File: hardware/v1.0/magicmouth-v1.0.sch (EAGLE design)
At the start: 36 parts, among them IC1 LM386N, IC2 ATMEGA328P_PDIP, J2 AUDIO-JACK2PTH, Q1 16Mhz, U1 ARDUINOR3-NOIOREF-NOTEXT

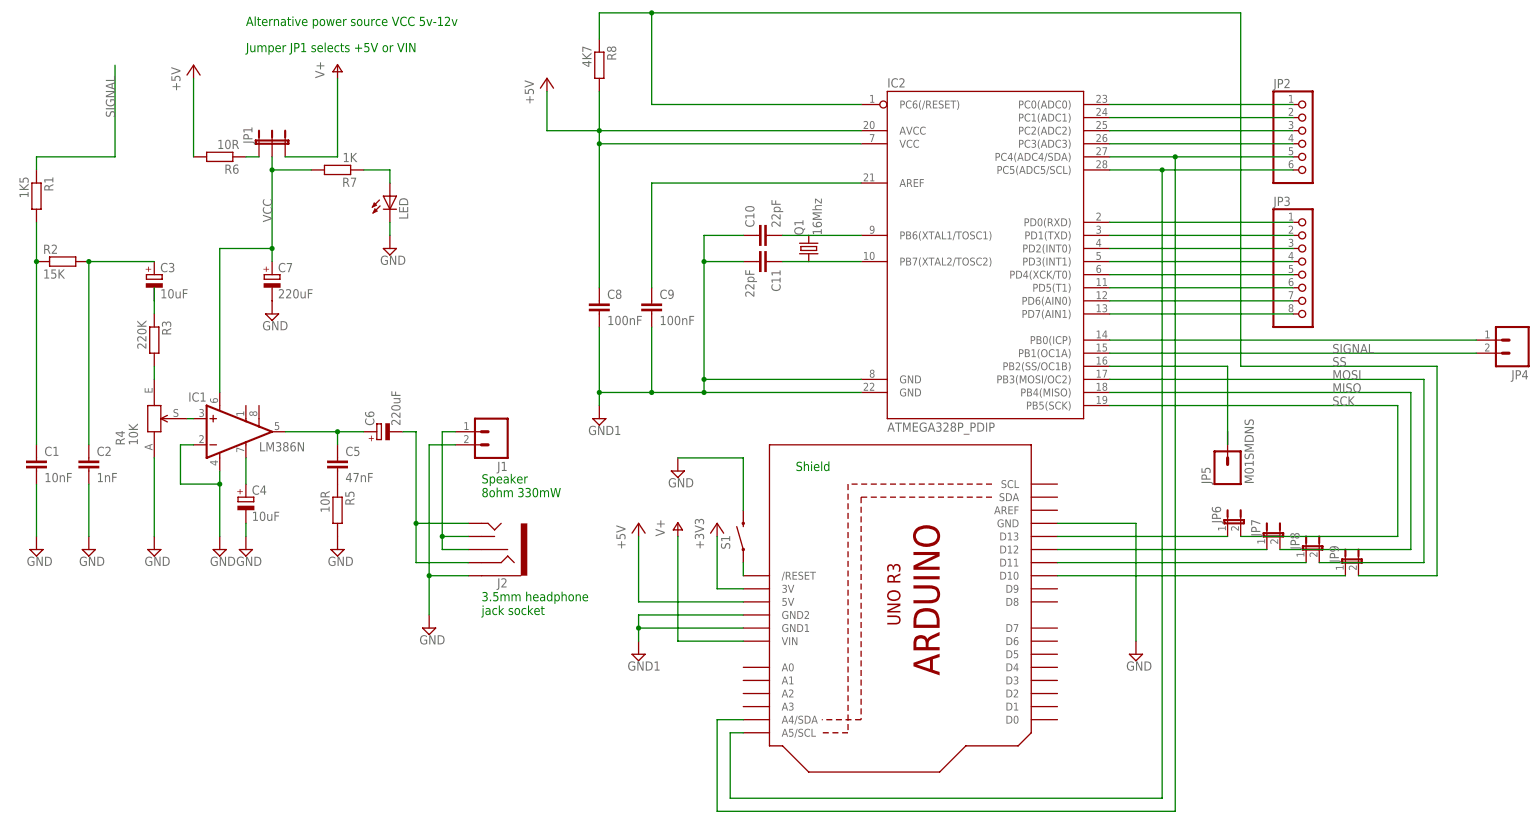
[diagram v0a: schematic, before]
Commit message: vias, isolated ground planes around crystal, gerbers
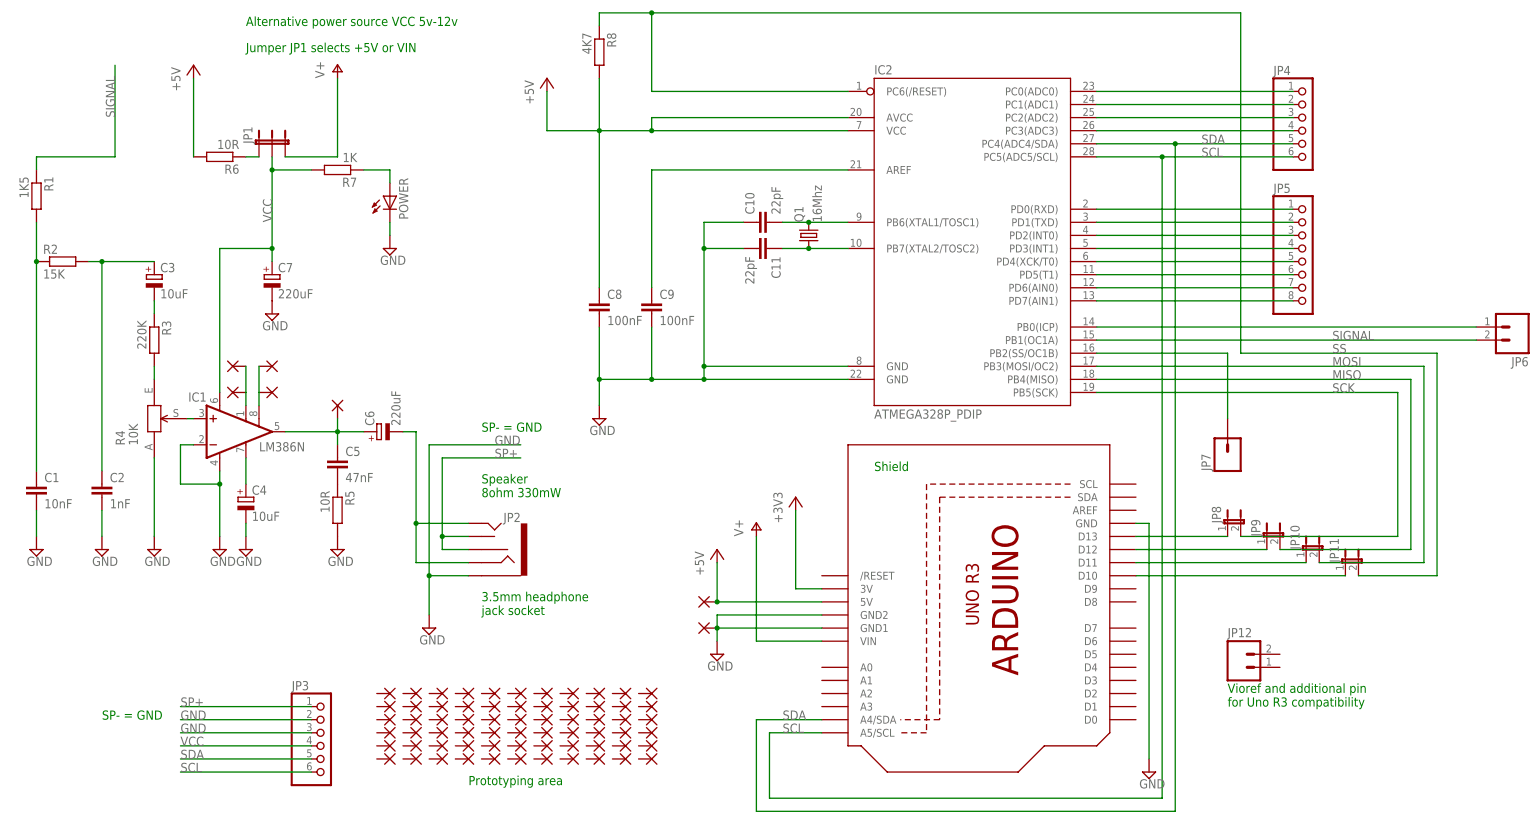
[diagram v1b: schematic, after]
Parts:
- removed J1: (no value), SparkFun-Connectors:M023.5MM
- removed J2: AUDIO-JACK2PTH, SparkFun-Connectors:AUDIO-JACK2PTH
- removed S1: SWITCH-MOMENTARY-2PTH, SparkFun-Electromechanical:SWITCH-MOMENTARY-2PTH
- added JP10, JP11: (no value), SparkFun-Passives:JUMPER-2PTH
- added JP12: (no value), SparkFun:M021X02_NO_SILK
- added P1, P5, P8, PAD1, PAD10, PAD11, PAD12, PAD13, PAD14, PAD15, PAD16, PAD17, PAD18, PAD19, PAD20, PAD21, PAD22, PAD23, PAD24, PAD25, PAD26, PAD27, PAD28, PAD29, PAD3, PAD30, PAD31, PAD32, PAD33, PAD34, PAD35, PAD36, PAD37, PAD38, PAD39, PAD40, PAD41, PAD42, PAD43, PAD44, PAD45, PAD46, PAD47, PAD48, PAD49, PAD50, PAD51, PAD52, PAD53, PAD54, PAD55, PAD56, PAD57, PAD58, PAD59, PAD60, PAD61, PAD62, PAD63, PAD64, PAD65, PAD66, PAD67, PAD68, PAD69, PAD7, PAD70, PAD71, PAD72, PAD73, PAD74, PAD8, PAD9: (no value), wirepad:1,6/0,8
- C1, C2, C5: device resistor:C-EU050-025X075 -> rcl:C-EU050-025X075
- C6, C7: device rcl:CPOL-EUTT5D7L -> rcl:CPOL-EUTT2D7
- JP2: value (none) -> AUDIO-JACK2PTH; device adafruit:PINHD-1X6CB -> SparkFun-Connectors:AUDIO-JACK2PTH
- JP3: device adafruit:PINHD-1X8CLEANBIG -> adafruit:PINHD-1X6CB
- JP4: device SparkFun-Connectors:M021X02_NO_SILK -> adafruit:PINHD-1X6CB
- JP5: value M01SMDNS -> (none); device SparkFun-Connectors:M01SMDNS -> adafruit:PINHD-1X8CLEANBIG
- JP6: device SparkFun-Passives:JUMPER-2PTH -> SparkFun-Connectors:M021X02_NO_SILK
- JP7: value (none) -> M01SMDNS; device SparkFun-Passives:JUMPER-2PTH -> SparkFun-Connectors:M01SMDNS
- R3: device rcl:R-EU_0207/7 -> resistor:R-EU_0207/7
- renumbered LED to POWER
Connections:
- removed net GND1: C10.1, C11.2, C8.2, C9.2, IC2.GND@1, IC2.GND@2, U1.GND1, U1.GND2
- removed net N$14 (its old number): IC2.PC1(ADC1), JP2.2
- removed net N$24 (its old number): IC2.PB0(ICP), JP4.1
- removed net N$25: JP6.1, U1.D13
- removed net N$26: JP7.1, U1.D12
- removed net N$27: IC2.PC3(ADC3), JP2.4
- removed net N$28: JP8.1, U1.D11
- removed net N$29: JP9.1, U1.D10
- removed net N$3 (its old number): J1.1, J2.RSH, J2.TSH
- removed net N$30: IC2.PC4(ADC4/SDA), JP2.5, U1.A4/SDA
- removed net N$31: IC2.PC5(ADC5/SCL), JP2.6, U1.A5/SCL
- removed net N$35: S1.1, U1./RESET
- new net D8: IC2.PB0(ICP), JP6.1
- new net N$101: IC1.GAIN@2, P8.P, PAD3.P
- new net N$32: IC2.PC2(ADC2), JP4.3
- new net N$33: IC2.PC3(ADC3), JP4.4
- new net N$58: IC1.GAIN@1, P1.P, PAD1.P
- new net N$90: JP8.1, U1.D13
- new net N$91: JP9.1, U1.D12
- new net N$92: JP10.1, U1.D11
- new net N$93: JP11.1, U1.D10
- new net SCL: IC2.PC5(ADC5/SCL), JP3.6, JP4.6, U1.A5/SCL
- new net SDA: IC2.PC4(ADC4/SDA), JP3.5, JP4.5, U1.A4/SDA
- new net SP+: JP2.RSH, JP2.TSH, JP3.1
- net +5V: now also PAD55.P
- net GND: now also C10.1, C11.2, C8.2, C9.2, IC2.GND@1, IC2.GND@2, JP2.SLEEVE, JP3.2, JP3.3, PAD68.P, U1.GND1, U1.GND2; no longer J1.2, J2.SLEEVE, S1.2
- net MISO: now also JP9.2; no longer JP7.2
- net MOSI: now also JP10.2; no longer JP8.2
- net N$1: now also P5.P
- net N$12: now also JP7.1; no longer JP5.1
- net N$13: now also JP4.1; no longer JP2.1
- net N$15: now also IC2.PC1(ADC1), JP4.2; no longer IC2.PC2(ADC2), JP2.3
- net N$16: now also JP5.1; no longer JP3.1
- net N$17: now also JP5.2; no longer JP3.2
- net N$18: now also JP5.3; no longer JP3.3
- net N$19: now also JP5.4; no longer JP3.4
- net N$20: now also JP5.5; no longer JP3.5
- net N$21: now also JP5.6; no longer JP3.6
- net N$22: now also JP5.7; no longer JP3.7
- net N$23: now also JP5.8; no longer JP3.8
- net N$8: now also JP2.RING, JP2.TIP; no longer J2.RING, J2.TIP
- net SCK: now also JP8.2; no longer JP6.2
- net SIGNAL: now also JP6.2; no longer JP4.2
- net SS: now also JP11.2; no longer JP9.2
- net VCC: now also JP3.4
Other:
- note added: "Prototyping area"
- note added: "SP- = GND"
- note added: "Vioref and additional pin for Uno R3 compatibility"
- moved on the sheet: C1, C10, C11, C2, IC2, JP8, JP9, Q1, R8

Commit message: pullup resistors on SDA and SCL
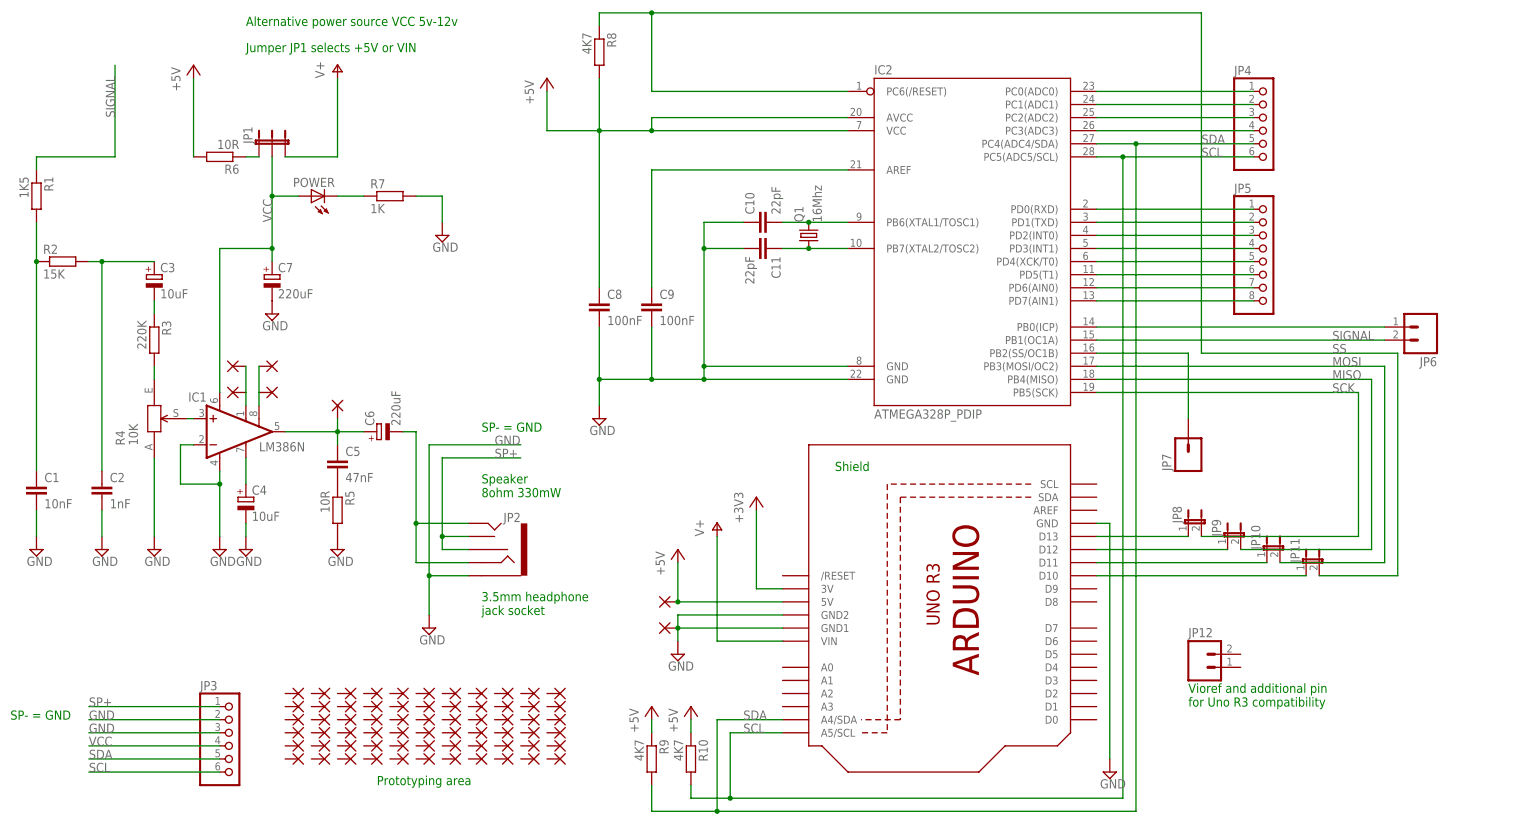
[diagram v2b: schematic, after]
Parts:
- added R10, R9: 4K7, rcl:R-EU_0207/7
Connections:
- net +5V: now also R10.1, R9.1
- net GND: now also R7.2; no longer POWER.C
- net N$10: now also POWER.C; no longer POWER.A
- net SCL: now also R10.2
- net SDA: now also R9.2
- net VCC: now also POWER.A; no longer R7.2
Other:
- moved on the sheet: JP10, JP11, JP12, JP3, JP4, JP5, JP6, JP7, JP8, JP9, POWER, R7
